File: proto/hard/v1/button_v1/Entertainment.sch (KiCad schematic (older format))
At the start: 44 parts, among them J6 Conn_01x08_Female, J8 AudioJack3, Q2 IRLML2060, Q4 IRLML2060, Q5 IRLML2060, U10 NL27WZ14, U5 RT9293, U8 485, U9 LM358

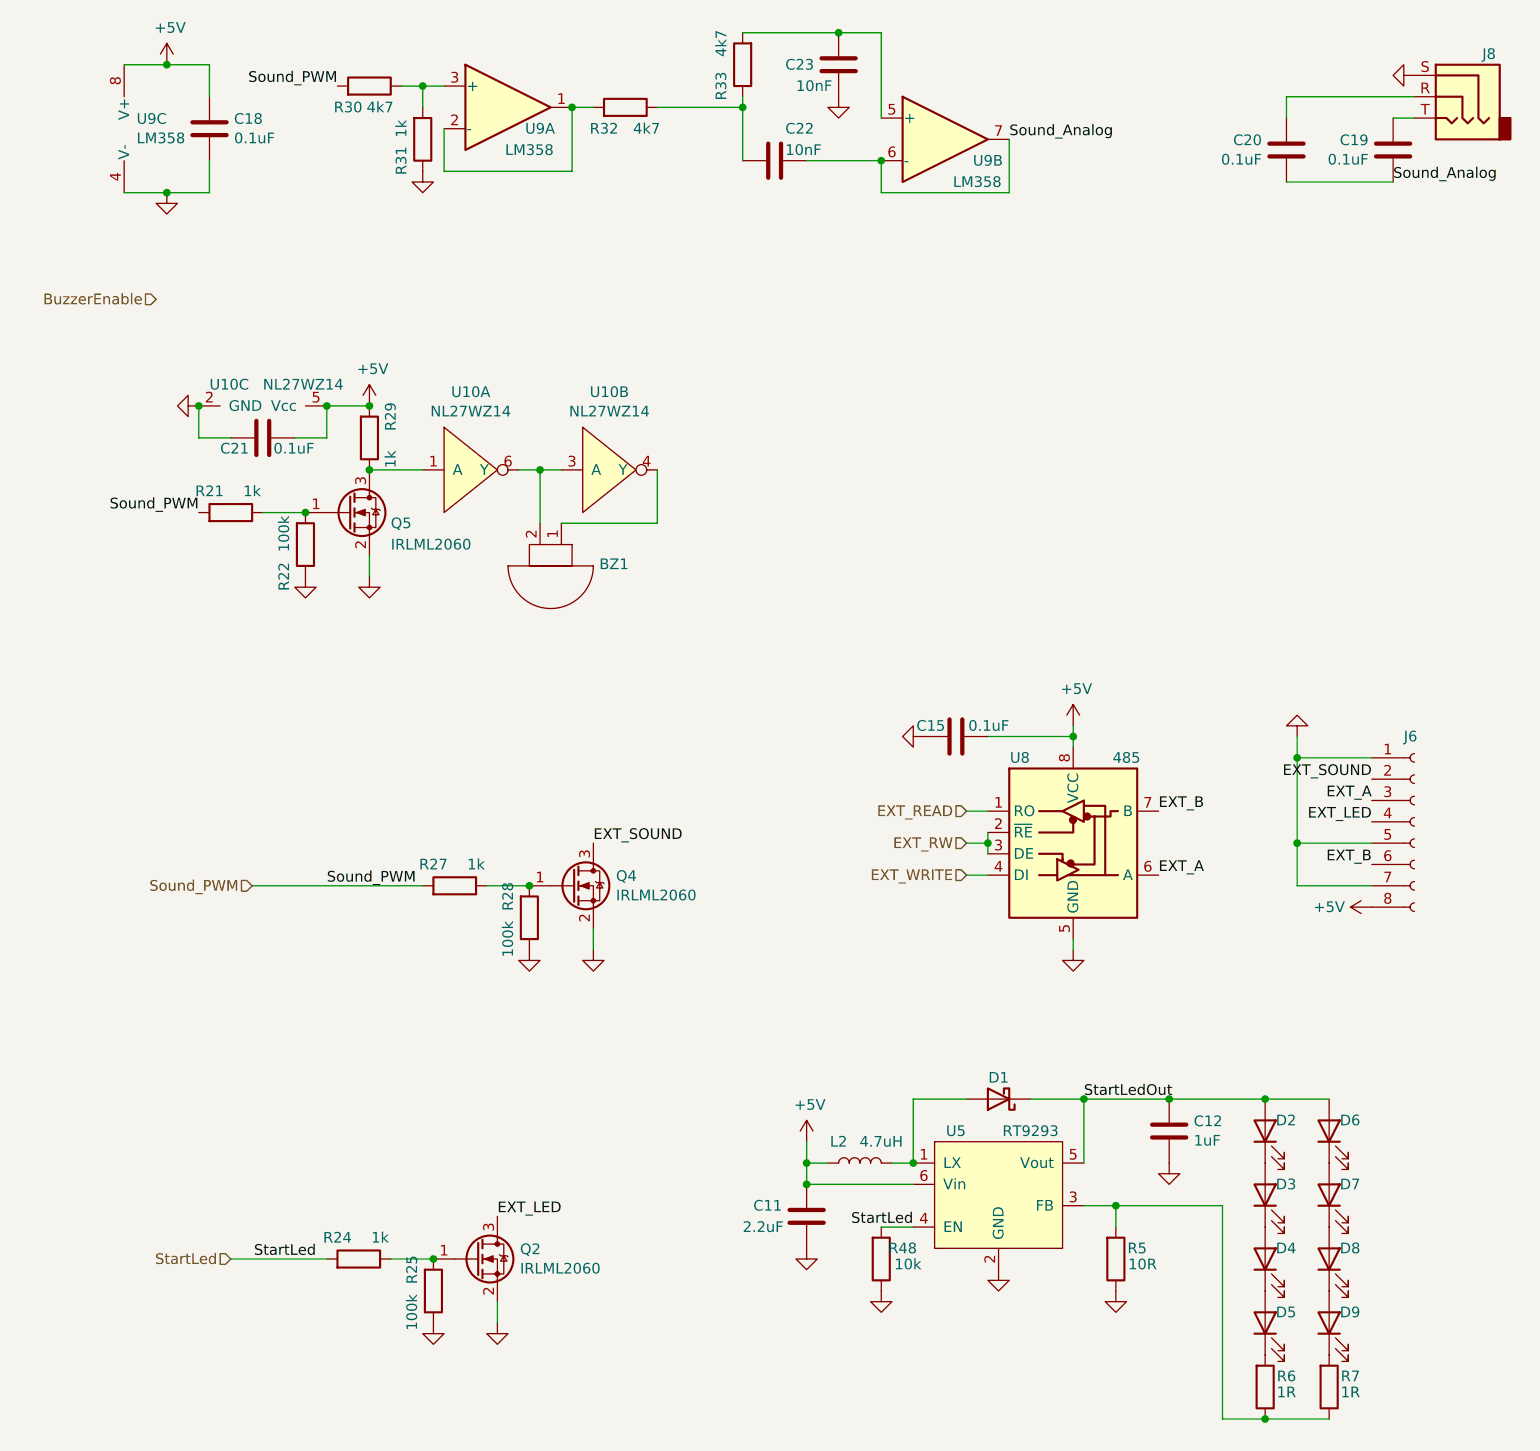
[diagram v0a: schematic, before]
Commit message: Rework of main board prototype. Work not finished.
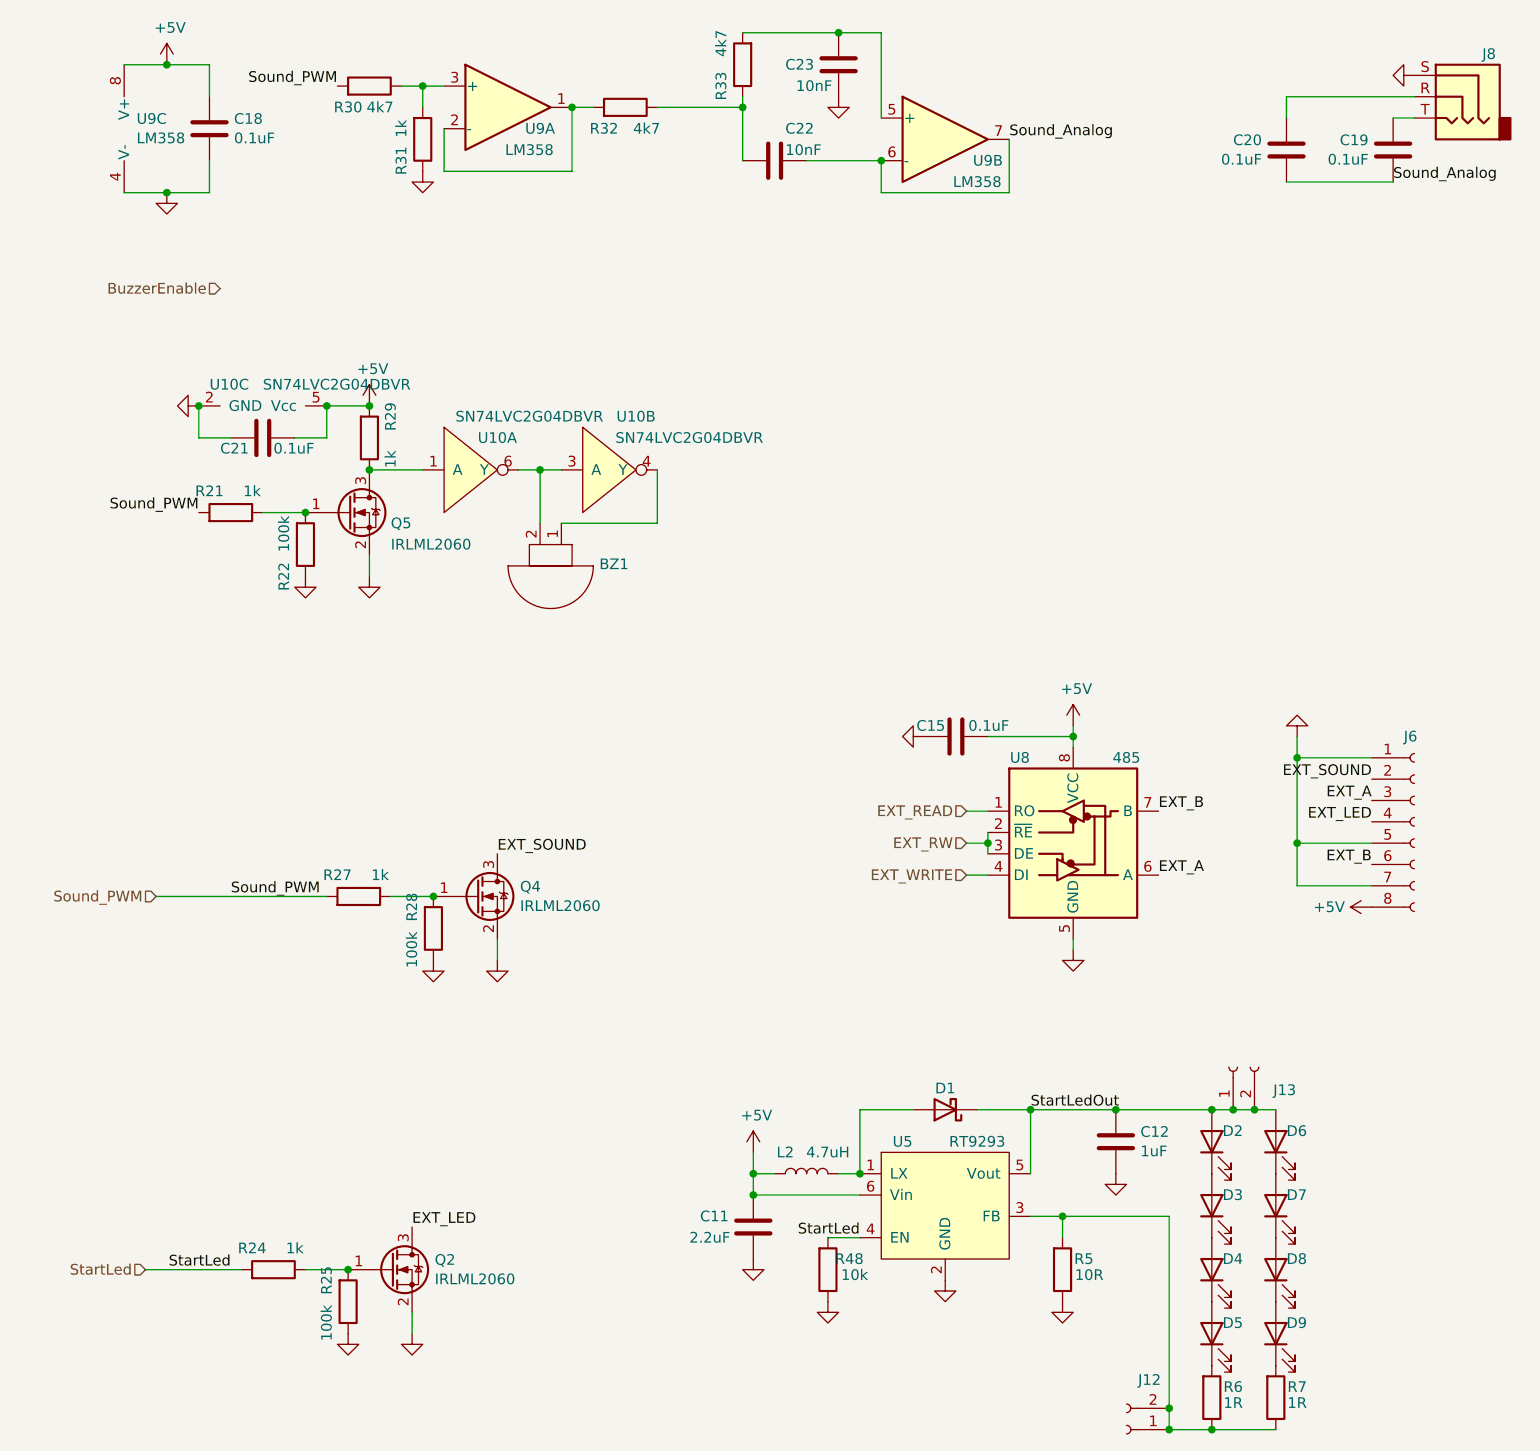
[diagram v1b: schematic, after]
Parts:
- added J12, J13: Conn_01x02_Female, Connector_PinHeader_2.54mm:PinHeader_1x02_P2.54mm_Vertical, symbol Connector:Conn_01x02_Female
- U10: value NL27WZ14 -> SN74LVC2G04DBVR
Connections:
- net StartLedOut: now also J13.1 (Pin_1), J13.2 (Pin_2)
- net at R5.2, R6.1, R7.1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: now also J12.1 (Pin_1), J12.2 (Pin_2)
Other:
- moved on the sheet: C11, C12, D1, D2, D3, D4, D5, D6, D7, D8, D9, L2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
